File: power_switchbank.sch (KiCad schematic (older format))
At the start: 12 parts, among them J1 CONN_02X01, J10 CONN_02X01, J11 CONN_02X01, J12 CONN_02X01, J2 CONN_02X01, J3 CONN_02X01, J4 CONN_02X01, J5 CONN_02X01, J6 CONN_02X01, J7 CONN_02X01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

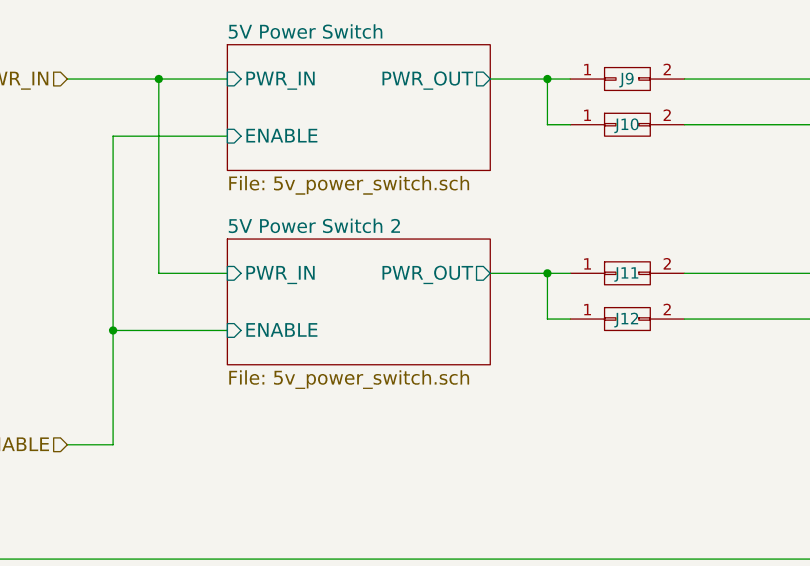
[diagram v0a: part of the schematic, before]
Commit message: add LEDs to indicate switch condition; fix hierarchical sheet issues
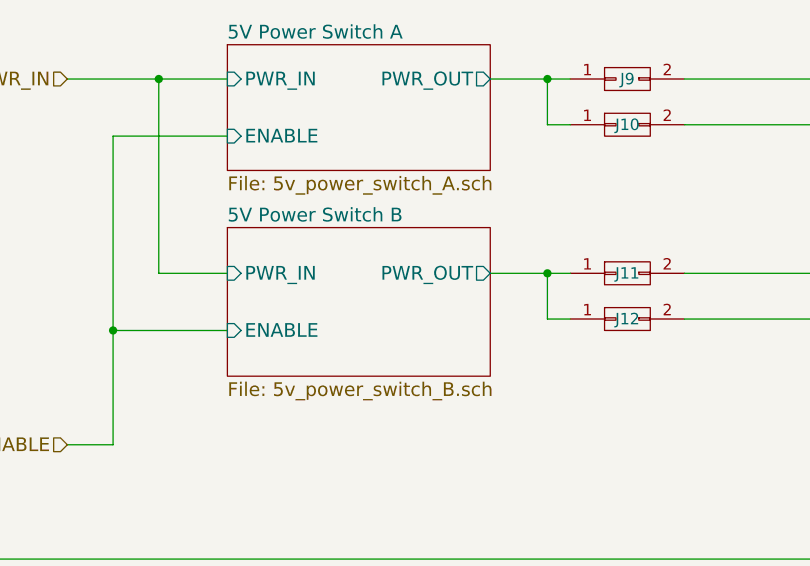
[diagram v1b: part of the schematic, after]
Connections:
- net 5V Power Switch 2/PWR_OUT renamed 5V Power Switch B/PWR_OUT
- net 5V Power Switch/PWR_OUT renamed 5V Power Switch A/PWR_OUT
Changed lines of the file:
@@
 S 7550 2850 1150 550
 U 59616167
-F0 "5V Power Switch" 60
-F1 "5v_power_switch.sch" 60
+F0 "5V Power Switch A" 60
+F1 "5v_power_switch_A.sch" 60
 F2 "PWR_IN" I L 7550 3000 60
 F3 "ENABLE" I L 7550 3250 60
@@
 	9550 3200 10150 3200
 Connection ~ 10150 3200
-$Sheet
-S 7550 3700 1150 550
-U 59651D34
-F0 "5V Power Switch 2" 60
-F1 "5v_power_switch.sch" 60
-F2 "PWR_IN" I L 7550 3850 60
-F3 "ENABLE" I L 7550 4100 60
-F4 "PWR_OUT" O R 8700 3850 60
-$EndSheet
 $Comp
 L CONN_02X01 J11
@@
 	5550 5100 10150 5100
 $Comp
-L PGND #PWR12
+L PGND #PWR012
 U 1 1 596573C9
 P 10150 5400
-F 0 "#PWR12" H 10020 5440 50  0001 L CNN
+F 0 "#PWR012" H 10020 5440 50  0001 L CNN
 F 1 "PGND" H 10150 5300 50  0000 C CNN
 F 2 "" H 10150 5400 60  0001 C CNN
@@
 	7250 3850 7550 3850
 Connection ~ 7250 3000
+$Sheet
+S 7550 3650 1150 650
+U 596B47A2
+F0 "5V Power Switch B" 60
+F1 "5v_power_switch_B.sch" 60
+F2 "PWR_OUT" O R 8700 3850 60
+F3 "PWR_IN" I L 7550 3850 60
+F4 "ENABLE" I L 7550 4100 60
+$EndSheet
 $EndSCHEMATC

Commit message: assign footprints to components
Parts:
- J1, J10, J11, J12, J2, J3, J4, J5, J6, J7, J8, J9: footprint (none) -> Connectors_Molex:Molex_MegaFit_2x01x5.70mm_Straight
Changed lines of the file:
@@
 F 0 "J7" H 4250 4050 50  0000 C CNN
 F 1 "CONN_02X01" H 4250 3850 50  0000 C CNN
-F 2 "" H 4250 2750 50  0001 C CNN
+F 2 "Connectors_Molex:Molex_MegaFit_2x01x5.70mm_Straight" H 4250 2750 50  0001 C CNN
 F 3 "" H 4250 2750 50  0001 C CNN
 	1    4250 3950
@@
 F 0 "J8" H 4250 4400 50  0000 C CNN
 F 1 "CONN_02X01" H 4250 4200 50  0000 C CNN
-F 2 "" H 4250 3100 50  0001 C CNN
+F 2 "Connectors_Molex:Molex_MegaFit_2x01x5.70mm_Straight" H 4250 3100 50  0001 C CNN
 F 3 "" H 4250 3100 50  0001 C CNN
 	1    4250 4300
@@
 F 0 "J1" H 4250 3000 50  0000 C CNN
 F 1 "CONN_02X01" H 4250 2900 50  0001 C CNN
-F 2 "" H 4250 1800 50  0001 C CNN
+F 2 "Connectors_Molex:Molex_MegaFit_2x01x5.70mm_Straight" H 4250 1800 50  0001 C CNN
 F 3 "" H 4250 1800 50  0001 C CNN
 	1    4250 3000
@@
 F 0 "J2" H 4250 3100 50  0000 C CNN
 F 1 "CONN_02X01" H 4250 3000 50  0001 C CNN
-F 2 "" H 4250 1900 50  0001 C CNN
+F 2 "Connectors_Molex:Molex_MegaFit_2x01x5.70mm_Straight" H 4250 1900 50  0001 C CNN
 F 3 "" H 4250 1900 50  0001 C CNN
 	1    4250 3100
@@
 F 0 "J3" H 4250 3200 50  0000 C CNN
 F 1 "CONN_02X01" H 4250 3100 50  0001 C CNN
-F 2 "" H 4250 2000 50  0001 C CNN
+F 2 "Connectors_Molex:Molex_MegaFit_2x01x5.70mm_Straight" H 4250 2000 50  0001 C CNN
 F 3 "" H 4250 2000 50  0001 C CNN
 	1    4250 3200
@@
 F 0 "J4" H 4250 3300 50  0000 C CNN
 F 1 "CONN_02X01" H 4250 3200 50  0001 C CNN
-F 2 "" H 4250 2100 50  0001 C CNN
+F 2 "Connectors_Molex:Molex_MegaFit_2x01x5.70mm_Straight" H 4250 2100 50  0001 C CNN
 F 3 "" H 4250 2100 50  0001 C CNN
 	1    4250 3300
@@
 F 0 "J5" H 4250 3400 50  0000 C CNN
 F 1 "CONN_02X01" H 4250 3300 50  0001 C CNN
-F 2 "" H 4250 2200 50  0001 C CNN
+F 2 "Connectors_Molex:Molex_MegaFit_2x01x5.70mm_Straight" H 4250 2200 50  0001 C CNN
 F 3 "" H 4250 2200 50  0001 C CNN
 	1    4250 3400
@@
 F 0 "J6" H 4250 3500 50  0000 C CNN
 F 1 "CONN_02X01" H 4250 3400 50  0001 C CNN
-F 2 "" H 4250 2300 50  0001 C CNN
+F 2 "Connectors_Molex:Molex_MegaFit_2x01x5.70mm_Straight" H 4250 2300 50  0001 C CNN
 F 3 "" H 4250 2300 50  0001 C CNN
 	1    4250 3500
@@
 F 0 "J9" H 9300 3000 50  0000 C CNN
 F 1 "CONN_02X01" H 9300 2900 50  0001 C CNN
-F 2 "" H 9300 1800 50  0001 C CNN
+F 2 "Connectors_Molex:Molex_MegaFit_2x01x5.70mm_Straight" H 9300 1800 50  0001 C CNN
 F 3 "" H 9300 1800 50  0001 C CNN
 	1    9300 3000
@@
 F 0 "J10" H 9300 3200 50  0000 C CNN
 F 1 "CONN_02X01" H 9300 3100 50  0001 C CNN
-F 2 "" H 9300 2000 50  0001 C CNN
+F 2 "Connectors_Molex:Molex_MegaFit_2x01x5.70mm_Straight" H 9300 2000 50  0001 C CNN
 F 3 "" H 9300 2000 50  0001 C CNN
 	1    9300 3200
@@
 F 0 "J11" H 9300 3850 50  0000 C CNN
 F 1 "CONN_02X01" H 9300 3750 50  0001 C CNN
-F 2 "" H 9300 2650 50  0001 C CNN
+F 2 "Connectors_Molex:Molex_MegaFit_2x01x5.70mm_Straight" H 9300 2650 50  0001 C CNN
 F 3 "" H 9300 2650 50  0001 C CNN
 	1    9300 3850
@@
 F 0 "J12" H 9300 4050 50  0000 C CNN
 F 1 "CONN_02X01" H 9300 3950 50  0001 C CNN
-F 2 "" H 9300 2850 50  0001 C CNN
+F 2 "Connectors_Molex:Molex_MegaFit_2x01x5.70mm_Straight" H 9300 2850 50  0001 C CNN
 F 3 "" H 9300 2850 50  0001 C CNN
 	1    9300 4050
